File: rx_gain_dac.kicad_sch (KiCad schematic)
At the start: 25 parts, among them U15 LMV358

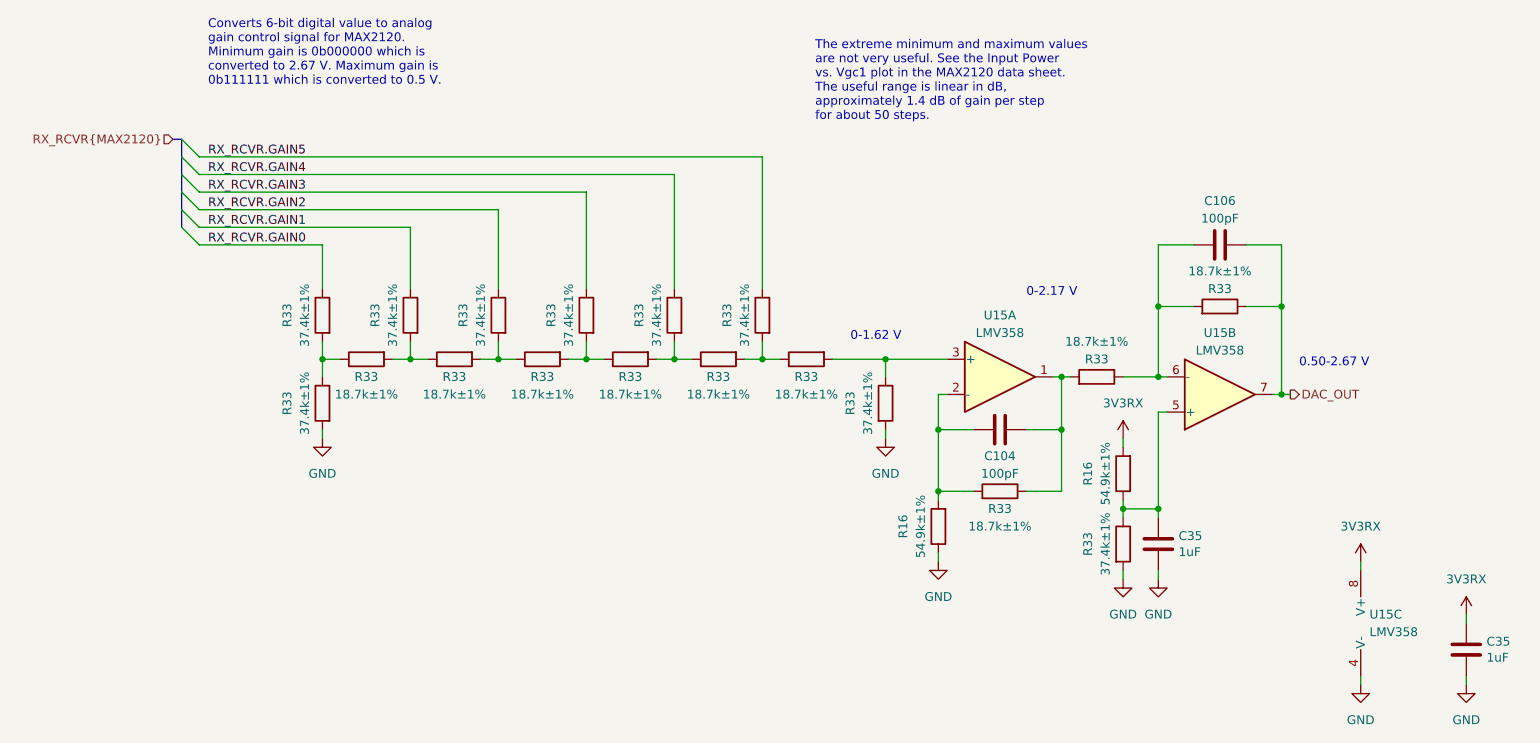
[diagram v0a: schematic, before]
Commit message: Replace open drain clock inverters with push-pull
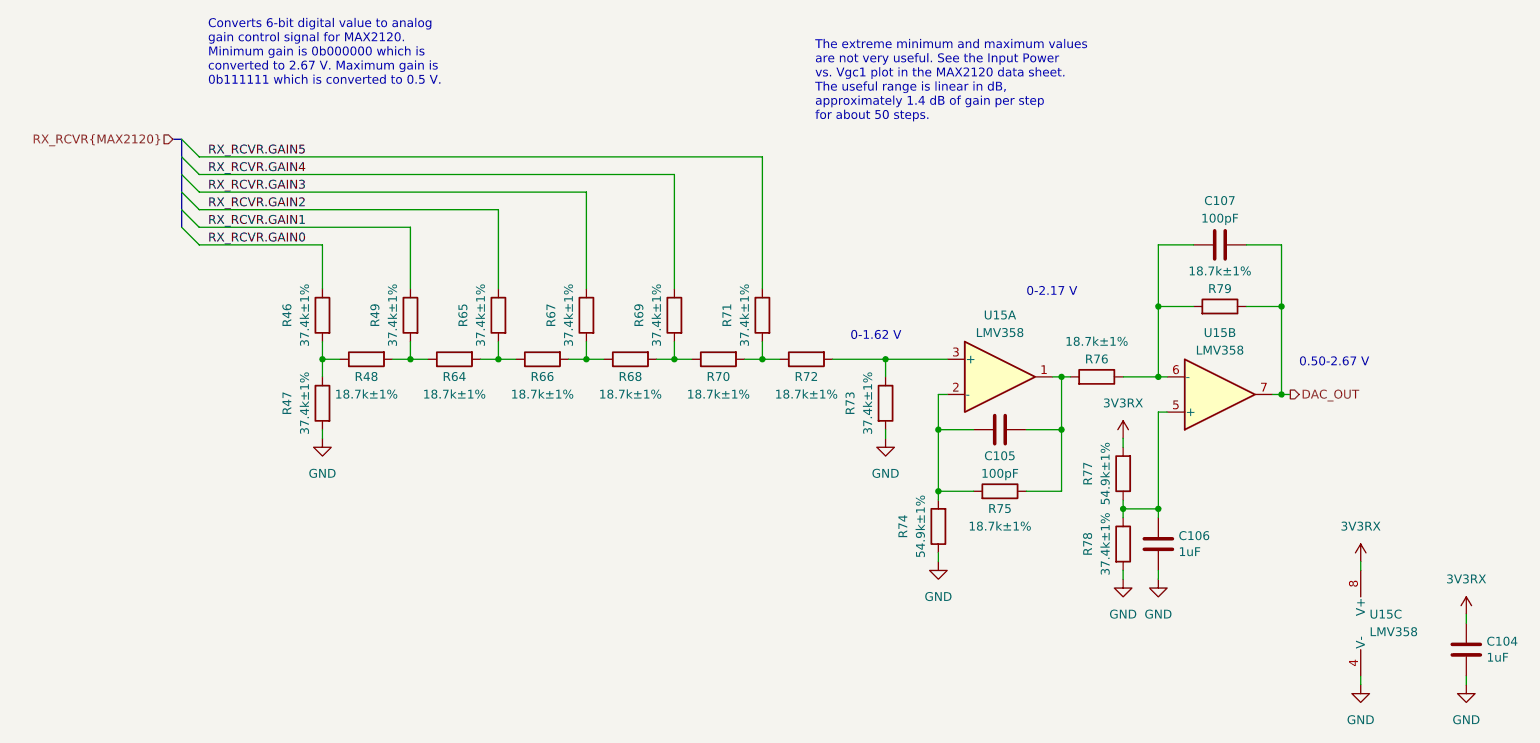
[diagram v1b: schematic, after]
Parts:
- renumbered C35 to C104, C104 to C105, C35 to C106, C106 to C107, R33 to R46, R33 to R47, R33 to R48, R33 to R49, R33 to R64, R33 to R65, R33 to R66, R33 to R67, R33 to R68, R33 to R69, R33 to R70, R33 to R71, R33 to R72, R33 to R73, R16 to R74, R33 to R75, R33 to R76, R16 to R77, R33 to R78, R33 to R79
